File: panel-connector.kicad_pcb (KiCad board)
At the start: 2 copper layers, 95.9 x 90.2 mm, 72 parts, among them J1 PC104-8BIT, J10 MOLEX_FFC-14, J11 MOLEX_FFC-14, J12 CONN-TAB, J13 CONN-TAB, J14 CONN-TAB, J15 CONN-TAB, J16 MOLEX_FFC-14, J18 CONN-TAB, J19 CONN-TAB, J2 PC104PTH, J20 CONN-TAB, J21 CONN-TAB, J22 MOLEX_FFC-14, J24 CONN-TAB, J25 CONN-TAB, J26 CONN-TAB, J27 CONN-TAB, J28 MOLEX_FFC-14, J3 PC104PTH, J4 PC104PTH, J5 PC104PTH, J6 CONN-TAB, J7 CONN-TAB, J8 CONN-TAB, J9 CONN-TAB, U1 ADG728, U10 SPV1040, U11 SPV1040, U12 SPV1040, U2 ADG728, U3 ADG728, U4 ADG728, U5 SPV1040, U6 SPV1040, U7 SPV1040, U8 SPV1040, U9 SPV1040

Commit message: populated mppt schematic and layed out mppt circuit
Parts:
- removed J10, J11, J16, J22, J28: MOLEX_FFC-14, SFUSat:MOLEX_FFC-14
- removed U1, U2, U3, U4: ADG728, SFUSat:TSSOP-16
- added C10: 4u7F, SFUSat-cap:C_0805, F.Cu at (269.2, 97.7)
- added C11: 10uF, SFUSat-cap:C_0805, F.Cu at (255.7, 120.0)
- added C12: 100nF, SFUSat-cap:C_0805, F.Cu at (264.3, 119.6)
- added C13: 1n0F, SFUSat-cap:C_0805, F.Cu at (260.2, 119.8)
- added C14: 1u0F, SFUSat-cap:C_0805, F.Cu at (255.4, 123.7)
- added C15: 10uF, SFUSat-cap:C_0805, F.Cu at (259.5, 124.1)
- added C16: 4u7F, SFUSat-cap:C_0805, F.Cu at (263.5, 124.0)
- added C17: 10uF, SFUSat-cap:C_0805, F.Cu at (53.1, 93.7)
- added C18: 100nF, SFUSat-cap:C_0805, F.Cu at (53.0, 96.9)
- added C19: 1n0F, SFUSat-cap:C_0805, F.Cu at (52.7, 100.8)
- added C20: 1u0F, SFUSat-cap:C_0805, F.Cu at (58.4, 93.5)
- added C21: 10uF, SFUSat-cap:C_0805, F.Cu at (57.8, 97.1)
- added C22: 4u7F, SFUSat-cap:C_0805, F.Cu at (57.0, 100.8)
- added C23: 10uF, SFUSat-cap:C_0805, F.Cu at (50.2, 124.6)
- added C24: 100nF, SFUSat-cap:C_0805, F.Cu at (50.4, 128.2)
- added C25: 1n0F, SFUSat-cap:C_0805, F.Cu at (55.1, 124.6)
- added C26: 1u0F, SFUSat-cap:C_0805, F.Cu at (55.7, 128.4)
- added C27: 10uF, SFUSat-cap:C_0805, F.Cu at (59.7, 124.2)
- added C28: 4u7F, SFUSat-cap:C_0805, F.Cu at (60.5, 128.2)
- added C29: 10uF, SFUSat-cap:C_0805, F.Cu at (129.0, 170.3)
- added C30: 100nF, SFUSat-cap:C_0805, F.Cu at (128.6, 174.2)
- added C31: 1n0F, SFUSat-cap:C_0805, F.Cu at (123.3, 170.5)
- added C32: 1u0F, SFUSat-cap:C_0805, F.Cu at (123.3, 175.0)
- added C33: 10uF, SFUSat-cap:C_0805, F.Cu at (118.5, 170.3)
- added C34: 4u7F, SFUSat-cap:C_0805, F.Cu at (117.6, 174.8)
- added C35: 10uF, SFUSat-cap:C_0805, F.Cu at (130.0, 189.2)
- added C36: 100nF, SFUSat-cap:C_0805, F.Cu at (129.4, 193.3)
- added C37: 1n0F, SFUSat-cap:C_0805, F.Cu at (123.7, 189.0)
- added C38: 1u0F, SFUSat-cap:C_0805, F.Cu at (123.3, 193.1)
- added C39: 10uF, SFUSat-cap:C_0805, F.Cu at (117.4, 189.2)
- added C40: 4u7F, SFUSat-cap:C_0805, F.Cu at (118.7, 193.4)
- added C41: 10uF, SFUSat-cap:C_0805, F.Cu at (119.6, 19.6)
- added C42: 100nF, SFUSat-cap:C_0805, F.Cu at (119.7, 24.3)
- added C43: 1n0F, SFUSat-cap:C_0805, F.Cu at (124.1, 19.6)
- added C44: 1u0F, SFUSat-cap:C_0805, F.Cu at (124.4, 23.7)
- added C45: 10uF, SFUSat-cap:C_0805, F.Cu at (128.9, 18.2)
- added C46: 4u7F, SFUSat-cap:C_0805, F.Cu at (129.5, 23.2)
- added C47: 10uF, SFUSat-cap:C_0805, F.Cu at (135.5, 71.5)
- added C48: 100nF, SFUSat-cap:C_0805, F.Cu at (136.5, 74.2)
- added C49: 1n0F, SFUSat-cap:C_0805, F.Cu at (144.7, 81.2)
- added C5: 10uF, SFUSat-cap:C_0805, F.Cu at (265.7, 94.5)
- added C50: 1u0F, SFUSat-cap:C_0805, F.Cu at (142.9, 77.4)
- added C51: 10uF, SFUSat-cap:C_0805, F.Cu at (143.7, 84.0)
- added C52: 4u7F, SFUSat-cap:C_0805, F.Cu at (137.4, 81.4)
- added C6: 100nF, SFUSat-cap:C_0805, F.Cu at (261.9, 94.3)
- added C7: 1n0F, SFUSat-cap:C_0805, F.Cu at (261.3, 97.9)
- added C8: 1u0F, SFUSat-cap:C_0805, F.Cu at (269.8, 94.5)
- added C9: 10uF, SFUSat-cap:C_0805, F.Cu at (265.1, 97.8)
- added D1: SMM4F5.0A-TR, SFUSat:SMM4F, F.Cu at (277.0, 88.8)
- added D2: SMM4F5.0A-TR, SFUSat:SMM4F, F.Cu at (274.3, 112.8)
- added D3: SMM4F5.0A-TR, SFUSat:SMM4F, F.Cu at (36.7, 90.7)
- added D4: SMM4F5.0A-TR, SFUSat:SMM4F, F.Cu at (41.9, 132.1)
- added D5: SMM4F5.0A-TR, SFUSat:SMM4F, F.Cu at (135.5, 177.1)
- added D6: SMM4F5.0A-TR, SFUSat:SMM4F, F.Cu at (144.4, 186.3)
- added D7: SMM4F5.0A-TR, SFUSat:SMM4F, F.Cu at (112.6, 28.1)
- added D8: SMM4F5.0A-TR, SFUSat:SMM4F, F.Cu at (133.0, 82.4)
- added L1: L_10u0_10%_1.42A_2-SMD,, SFUSat-ind:L_2220, F.Cu at (260.3, 88.6)
- added L2: L_10u0_10%_1.42A_2-SMD,, SFUSat-ind:L_2220, F.Cu at (258.9, 113.3)
- added L3: L_10u0_10%_1.42A_2-SMD,, SFUSat-ind:L_2220, F.Cu at (35.2, 83.7)
- added L4: L_10u0_10%_1.42A_2-SMD,, SFUSat-ind:L_2220, F.Cu at (32.7, 126.2)
- added L5: L_10u0_10%_1.42A_2-SMD,, SFUSat-ind:L_2220, F.Cu at (146.9, 172.0)
- added L6: L_10u0_10%_1.42A_2-SMD,, SFUSat-ind:L_2220, F.Cu at (146.3, 192.7)
- added L7: L_10u0_10%_1.42A_2-SMD,, SFUSat-ind:L_2220, F.Cu at (101.6, 22.9)
- added L8: L_10u0_10%_1.42A_2-SMD,, SFUSat-ind:L_2220, F.Cu at (130.7, 76.7)
- added R27: 1K, SFUSat-res:R_0805, F.Cu at (274.1, 84.1)
- added R28: 0R, SFUSat-res:R_0402, F.Cu at (264.8, 79.6)
- added R29: 1k0, SFUSat-res:R_0805, F.Cu at (264.8, 82.0)
- added R30: 1k0, SFUSat-res:R_0805, F.Cu at (268.9, 79.3)
- added R31: 10m0, SFUSat-res:R_1206, F.Cu at (268.4, 81.4)
- added R32: 1M0, SFUSat-res:R_0805, F.Cu at (264.7, 83.8)
- added R33: 357k, SFUSat-res:R_0805, F.Cu at (268.6, 83.5)
- added R34: 1K, SFUSat-res:R_0805, F.Cu at (271.7, 117.9)
- added R35: 0R, SFUSat-res:R_0402, F.Cu at (274.6, 117.7)
- added R36: 1k0, SFUSat-res:R_0805, F.Cu at (277.5, 117.7)
- added R37: 1k0, SFUSat-res:R_0805, F.Cu at (271.9, 119.7)
- added R38: 10m0, SFUSat-res:R_1206, F.Cu at (276.1, 120.1)
- added R39: 1M0, SFUSat-res:R_0805, F.Cu at (271.5, 121.9)
- added R40: 357k, SFUSat-res:R_0805, F.Cu at (275.1, 122.2)
- added R41: 1K, SFUSat-res:R_0805, F.Cu at (35.4, 105.2)
- added R42: 0R, SFUSat-res:R_0402, F.Cu at (35.6, 103.7)
- added R43: 1k0, SFUSat-res:R_0805, F.Cu at (38.7, 103.4)
- added R44: 1k0, SFUSat-res:R_0805, F.Cu at (39.2, 105.1)
- added R45: 10m0, SFUSat-res:R_1206, F.Cu at (31.2, 104.7)
- added R46: 1M0, SFUSat-res:R_0805, F.Cu at (34.9, 102.4)
- added R47: 357k, SFUSat-res:R_0805, F.Cu at (31.5, 102.2)
- added R48: 1K, SFUSat-res:R_0805, F.Cu at (32.6, 134.1)
- added R49: 0R, SFUSat-res:R_0402, F.Cu at (29.8, 134.1)
- added R50: 1k0, SFUSat-res:R_0805, F.Cu at (36.0, 133.9)
- added R51: 1k0, SFUSat-res:R_0805, F.Cu at (35.9, 135.6)
- added R52: 10m0, SFUSat-res:R_1206, F.Cu at (32.4, 135.8)
- added R53: 1M0, SFUSat-res:R_0805, F.Cu at (28.7, 135.7)
- added R54: 357k, SFUSat-res:R_0805, F.Cu at (36.2, 137.2)
- added R55: 1K, SFUSat-res:R_0805, F.Cu at (129.5, 160.6)
- added R56: 0R, SFUSat-res:R_0402, F.Cu at (131.9, 160.4)
- added R57: 1k0, SFUSat-res:R_0805, F.Cu at (129.1, 162.3)
- added R58: 1k0, SFUSat-res:R_0805, F.Cu at (132.6, 162.2)
- added R59: 10m0, SFUSat-res:R_1206, F.Cu at (135.4, 160.4)
- added R60: 1M0, SFUSat-res:R_0805, F.Cu at (135.8, 162.3)
- added R61: 357k, SFUSat-res:R_0805, F.Cu at (126.0, 162.2)
- added R62: 1K, SFUSat-res:R_0805, F.Cu at (102.9, 190.7)
- added R63: 0R, SFUSat-res:R_0402, F.Cu at (109.0, 190.2)
- added R64: 1k0, SFUSat-res:R_0805, F.Cu at (106.5, 190.7)
- added R65: 1k0, SFUSat-res:R_0805, F.Cu at (111.7, 190.6)
- added R66: 10m0, SFUSat-res:R_1206, F.Cu at (102.3, 192.6)
- added R67: 1M0, SFUSat-res:R_0805, F.Cu at (105.9, 192.5)
- added R68: 357k, SFUSat-res:R_0805, F.Cu at (109.4, 192.6)
- added R69: 1K, SFUSat-res:R_0805, F.Cu at (102.0, 32.6)
- added R70: 0R, SFUSat-res:R_0402, F.Cu at (104.8, 32.0)
- added R71: 1k0, SFUSat-res:R_0805, F.Cu at (114.0, 31.9)
- added R72: 1k0, SFUSat-res:R_0805, F.Cu at (110.4, 33.1)
- added R73: 10m0, SFUSat-res:R_1206, F.Cu at (105.7, 34.7)
- added R74: 1M0, SFUSat-res:R_0805, F.Cu at (109.9, 35.2)
- added R75: 357k, SFUSat-res:R_0805, F.Cu at (113.8, 35.3)
- added R76: 1K, SFUSat-res:R_0805, F.Cu at (134.5, 74.2)
- added R77: 0R, SFUSat-res:R_0402, F.Cu at (139.6, 75.5)
- added R78: 1k0, SFUSat-res:R_0805, F.Cu at (145.8, 76.5)
- added R79: 1k0, SFUSat-res:R_0805, F.Cu at (145.8, 78.4)
- added R80: 10m0, SFUSat-res:R_1206, F.Cu at (137.9, 83.6)
- added R81: 1M0, SFUSat-res:R_0805, F.Cu at (142.7, 81.2)
- added R82: 357k, SFUSat-res:R_0805, F.Cu at (146.6, 81.2)
- moved U12 54.9 mm to (137.5, 78.1)
- moved U8 23.0 mm to (42.8, 126.0)
- moved U10 13.6 mm to (137.4, 192.3)
- moved U6 12.8 mm to (268.0, 112.7)
- moved U7 8.33 mm to (44.6, 86.7)
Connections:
- net /3V3 renamed /Port_X+/3V3
- net /SCL renamed /Port_X+/SCL
- net /SDA renamed /Port_X+/SDA
- net /SENSOR_X+ renamed /Port_X+/SUN_SENSOR
- net /SENSOR_X- renamed /Port_X-/SUN_SENSOR
- net /SENSOR_Y+ renamed /Port_Y+/SUN_SENSOR
- net /SENSOR_Y- renamed /Port_Y-/SUN_SENSOR
- U11 pad 2: GND -> /MPPT_Y-_1/PV-
- U5 pad 2: GND -> /MPPT_X+_1/PV-
- U7 pad 2: GND -> /MPPT_X-_1/PV-
- U9 pad 2: GND -> /MPPT_Y+_1/PV-
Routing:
- net Net-(C52-Pad1): track 0.00 -> 17.4 mm, vias 0 -> 2
- net /MPPT_Y-_1/PV-: track 0.00 -> 10.7 mm, vias 0 -> 2
- net GND: track 0.00 -> 9.21 mm, vias 0 -> 8
- net Net-(C49-Pad1): track 0.00 -> 6.69 mm
- net Net-(C48-Pad1): track 0.00 -> 6.64 mm
- net Net-(C50-Pad1): track 0.00 -> 4.89 mm
- net Net-(C50-Pad2): track 0.00 -> 4.32 mm
- net Net-(R77-Pad1): track 0.00 -> 1.78 mm
- added copper zone on F.Cu, net /MPPT_Y-_1/PV-
- added copper zone on F.Cu, net /MPPT_Y-_2/PV+
- added copper zone on B.Cu, net GND
- added copper zone on F.Cu, net Net-(C52-Pad1)
- added copper zone on F.Cu, net Net-(L8-Pad2)
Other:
- net class PV_PWR added: clearance 0.2, trace_width 0.4, via_dia 0.6, via_drill 0.4
- rule trace_min: 0.2 -> 0.1524

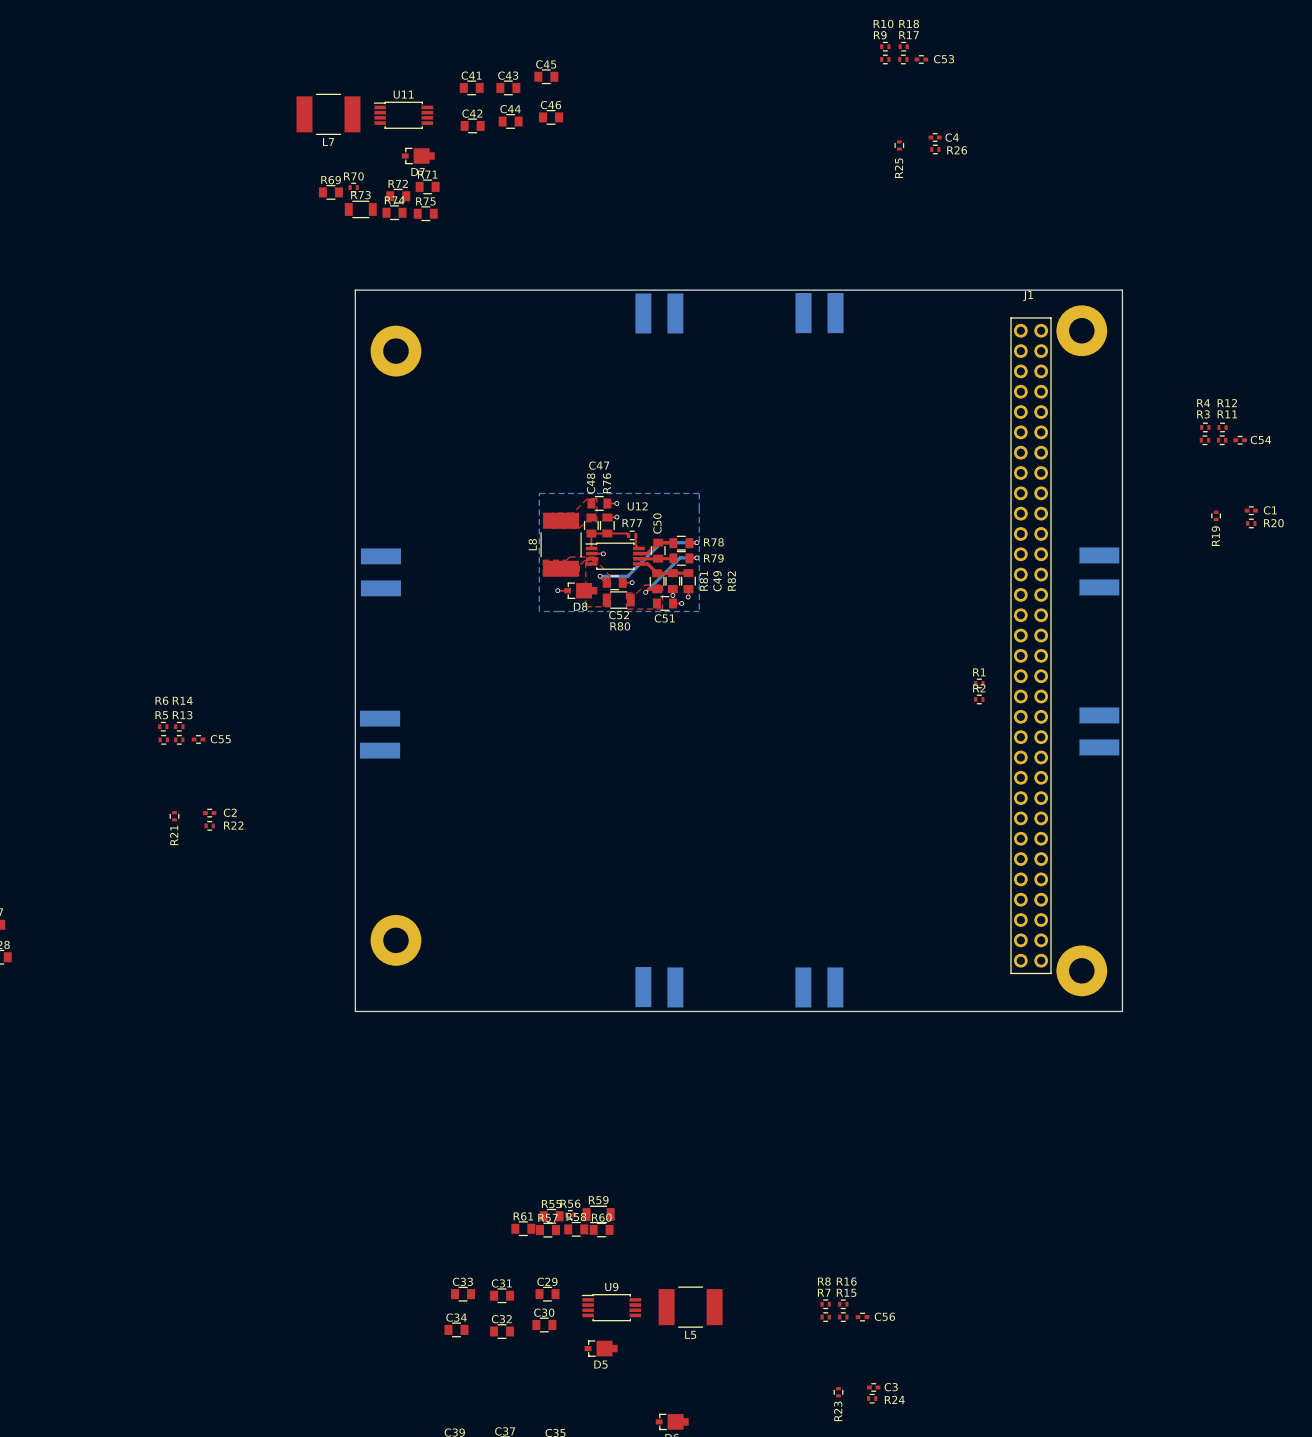
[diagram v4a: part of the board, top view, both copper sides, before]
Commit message: Added decoupling to connector
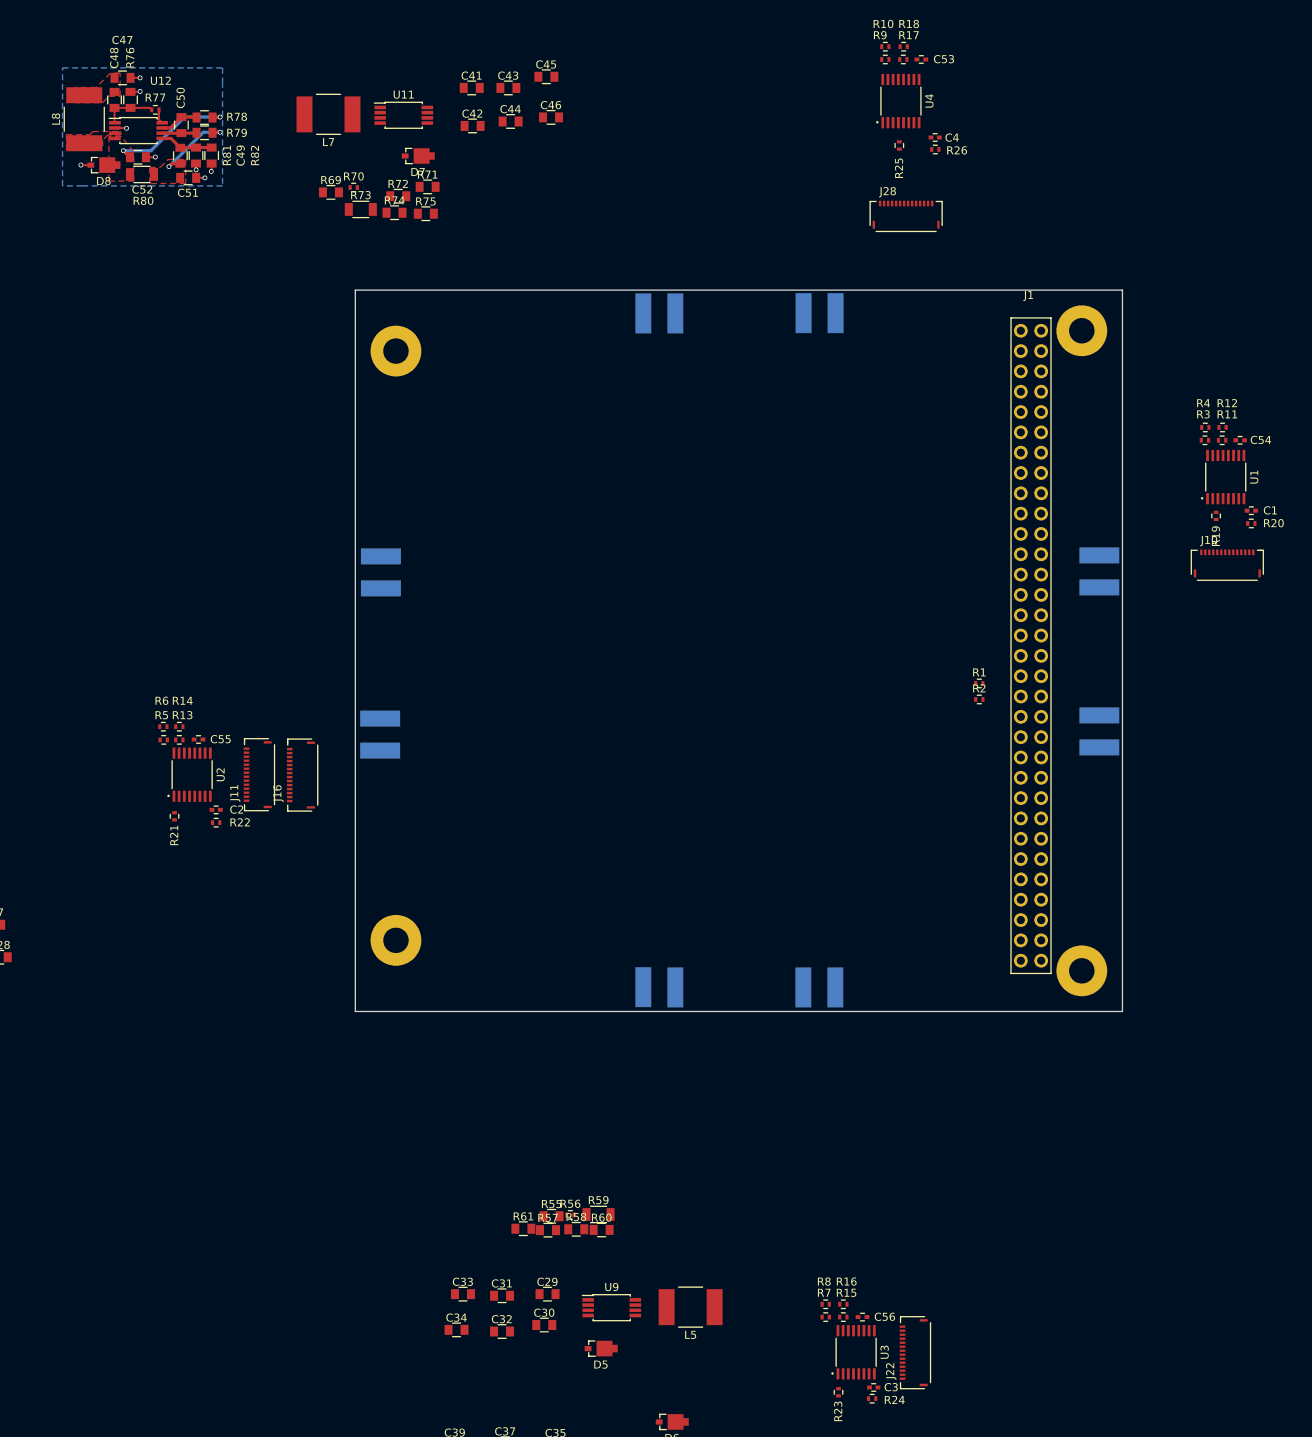
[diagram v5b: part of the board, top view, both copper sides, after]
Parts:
- added J10: MOLEX_FFC-14, SFUSat:MOLEX_FFC-14, F.Cu at (214.0, 77.6)
- added J11: MOLEX_FFC-14, SFUSat:MOLEX_FFC-14, F.Cu at (91.4, 105.4)
- added J16: MOLEX_FFC-14, SFUSat:MOLEX_FFC-14, F.Cu at (96.8, 105.5)
- added J22: MOLEX_FFC-14, SFUSat:MOLEX_FFC-14, F.Cu at (173.4, 177.7)
- added J28: MOLEX_FFC-14, SFUSat:MOLEX_FFC-14, F.Cu at (173.8, 34.0)
- added U1: ADG728, SFUSat:TSSOP-16, F.Cu at (213.8, 68.2)
- added U2: ADG728, SFUSat:TSSOP-16, F.Cu at (84.6, 105.4)
- added U3: ADG728, SFUSat:TSSOP-16, F.Cu at (167.6, 177.6)
- added U4: ADG728, SFUSat:TSSOP-16, F.Cu at (173.2, 21.2)
- moved C49 79.9 mm to (85.1, 28.0)
- moved C50 79.9 mm to (83.3, 24.2)
- moved C52 79.9 mm to (77.8, 28.2)
- moved L8 79.9 mm to (71.1, 23.5)
- moved R79 79.9 mm to (86.2, 25.2)
- moved R78 79.9 mm to (86.2, 23.3)
- moved U12 79.9 mm to (77.9, 24.9)
- moved C47 79.9 mm to (75.9, 18.3)
- moved C48 79.9 mm to (76.9, 21.1)
- moved C51 79.9 mm to (84.1, 30.8)
- moved D8 79.9 mm to (73.4, 29.2)
- moved R76 79.9 mm to (74.9, 21.1)
- moved R77 79.9 mm to (80.0, 22.3)
- moved R80 79.9 mm to (78.3, 30.4)
- moved R81 79.9 mm to (83.1, 28.0)
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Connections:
- net /Port_X+/3V3 renamed /3V3
- net /Port_X+/SCL renamed /SCL
- net /Port_X+/SDA renamed /SDA
- net /Port_X+/SUN_SENSOR renamed /SENSOR_X+
- net /Port_X-/SUN_SENSOR renamed /SENSOR_X-
- net /Port_Y+/SUN_SENSOR renamed /SENSOR_Y+
- net /Port_Y-/SUN_SENSOR renamed /SENSOR_Y-

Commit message: layed out MPPT
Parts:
- removed C10: 4u7F, SFUSat-cap:C_0805
- removed C5, C9: 10uF, SFUSat-cap:C_0805
- removed C6: 100nF, SFUSat-cap:C_0805
- removed C7: 1n0F, SFUSat-cap:C_0805
- removed C8: 1u0F, SFUSat-cap:C_0805
- added C100: 10uF, SFUSat-cap:C_0805, F.Cu at (249.9, -19.7)
- added C101: 100nF, SFUSat-cap:C_0805, F.Cu at (250.9, -16.9)
- added C102: 1n0F, SFUSat-cap:C_0805, F.Cu at (259.1, -9.95)
- added C103: 1u0F, SFUSat-cap:C_0805, F.Cu at (257.3, -13.8)
- added C104: 10uF, SFUSat-cap:C_0805, F.Cu at (258.1, -7.16)
- added C105: 4u7F, SFUSat-cap:C_0805, F.Cu at (251.8, -9.74)
- added C200: DNP, Capacitors_SMD:C_0402, F.Cu at (261.5, 68.0)
- added C203: DNP, Capacitors_SMD:C_0402, F.Cu at (254.5, 68.0)
- added C210: DNP, Capacitors_SMD:C_0402, F.Cu at (261.3, 97.9)
- added C213: DNP, Capacitors_SMD:C_0402, F.Cu at (269.8, 94.5)
- added C220: DNP, Capacitors_SMD:C_0402, F.Cu at (265.1, 97.8)
- added C223: DNP, Capacitors_SMD:C_0402, F.Cu at (269.2, 97.7)
- added C230, C233: DNP, Capacitors_SMD:C_0402, F.Cu at (152.9, 145.1)
- moved L150 232.5 mm to (85.1, -31.5), turned to 270 degrees
- moved C151 230.5 mm to (90.9, -34.0), turned to 90 degrees
- moved C150 229.5 mm to (89.9, -36.7)
- moved U150 227.0 mm to (91.9, -30.1)
- moved C153 225.4 mm to (97.3, -30.8), turned to 270 degrees
- moved R150 225.1 mm to (88.9, -34.0), turned to 270 degrees
- moved R151 223.4 mm to (94.0, -32.7), turned to 180 degrees
- moved R152 222.5 mm to (100.2, -31.7), turned to 180 degrees
- moved C155 221.9 mm to (91.8, -26.8)
- moved R153 220.7 mm to (100.2, -29.8), turned to 180 degrees
- moved R131 220.5 mm to (174.0, -32.7), turned to 180 degrees
- moved R135 220.2 mm to (177.1, -27.0), turned to 90 degrees
- moved R156 219.8 mm to (101.0, -27.0), turned to 270 degrees
- moved D150 219.6 mm to (87.4, -25.8)
- moved R132 219.6 mm to (180.2, -31.7), turned to 180 degrees
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- renumbered C11 to C110, C12 to C111, C13 to C112, C14 to C113, C15 to C114, C16 to C115, C17 to C120, C18 to C121, C19 to C122, C20 to C123, C21 to C124, C22 to C125, C23 to C130, C24 to C131, C25 to C132, C26 to C133, C27 to C134, C28 to C135, C29 to C140, C30 to C141, C31 to C142, C32 to C143, C33 to C144, C34 to C145, C35 to C150, C36 to C151, C37 to C152, C38 to C153, C39 to C154, C40 to C155, C41 to C160, C42 to C161, C43 to C162, C44 to C163, C45 to C164, C46 to C165, C47 to C170, C48 to C171, C49 to C172, C50 to C173, C51 to C174, C52 to C175, C54 to C201, C1 to C202, C55 to C211, C2 to C212, C56 to C221, C3 to C222, C53 to C231, C4 to C232, D1 to D100, D2 to D110, D3 to D120, D4 to D130, D5 to D140, D6 to D150, D7 to D160, D8 to D170, J11 to J105, J10 to J200, J6 to J201, J7 to J202, J8 to J203, J9 to J204, J16 to J210, J12 to J211, J13 to J212, J14 to J213, J15 to J214, J22 to J220, J18 to J221, J19 to J222, J20 to J223, J21 to J224, J28 to J230, J24 to J231, J25 to J232, J26 to J233, J27 to J234, L1 to L100, L2 to L110, L3 to L120, L4 to L130, L5 to L140, L6 to L150, L7 to L160, L8 to L170, R27 to R100, R28 to R101, R29 to R102, R30 to R103, R31 to R104, R32 to R105, R33 to R106, R34 to R110, R35 to R111, R36 to R112, R37 to R113, R38 to R114, R39 to R115, R40 to R116, R41 to R120, R42 to R121, R43 to R122, R44 to R123, R45 to R124, R46 to R125, R47 to R126, R48 to R130, R49 to R131, R50 to R132, R51 to R133, R52 to R134, R53 to R135, R54 to R136, R55 to R140, R56 to R141, R57 to R142, R58 to R143, R59 to R144, R60 to R145, R61 to R146, R62 to R150, R63 to R151, R64 to R152, R65 to R153, R66 to R154, R67 to R155, R68 to R156, R69 to R160, R70 to R161, R71 to R162, R72 to R163, R73 to R164, R74 to R165, R75 to R166, R76 to R170, R77 to R171, R78 to R172, R79 to R173, R80 to R174, R81 to R175, R82 to R176, R20 to R200, R19 to R201'1, R3 to R202, R11 to R203, R4 to R204, R12 to R205, R22 to R210, R21 to R211, R5 to R212, R13 to R213, R6 to R214, R14 to R215, R24 to R220, R23 to R221, R7 to R222, R15 to R223, R8 to R224, R16 to R225, R26 to R230, R25 to R231, R9 to R232, R17 to R233, R10 to R234, R18 to R235, U5 to U100, U6 to U110, U7 to U120, U8 to U130, U9 to U140, U10 to U150, U11 to U160, U12 to U170, U1 to U200, U2 to U210, U3 to U220, U4 to U230
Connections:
- net Net-(L1-Pad2) renamed /MPPT_X+_1/LX
- net Net-(L2-Pad2) renamed /MPPT_X+_2/LX
- net Net-(L3-Pad2) renamed /MPPT_X-_1/LX
- net Net-(L4-Pad2) renamed /MPPT_X-_2/LX
- net Net-(L5-Pad2) renamed /MPPT_Y+_1/LX
- net Net-(L6-Pad2) renamed /MPPT_Y+_2/LX
- net Net-(L7-Pad2) renamed /MPPT_Y-_1/LX
- net Net-(L8-Pad2) renamed /MPPT_Y-_2/LX
- C113 pad 1: Net-(C14-Pad1) -> Net-(C113-Pad1)
- C113 pad 2: Net-(C14-Pad2) -> Net-(C113-Pad2)
- C115 pad 1: Net-(C16-Pad1) -> /MPPT_X+_2/MPPT_OUT
- C123 pad 1: Net-(C20-Pad1) -> Net-(C123-Pad1)
- C123 pad 2: Net-(C20-Pad2) -> Net-(C123-Pad2)
- C125 pad 1: Net-(C22-Pad1) -> /MPPT_X-_1/MPPT_OUT
- C133 pad 1: Net-(C26-Pad1) -> Net-(C133-Pad1)
- C133 pad 2: Net-(C26-Pad2) -> Net-(C133-Pad2)
- C135 pad 1: Net-(C28-Pad1) -> /MPPT_X-_2/MPPT_OUT
- C143 pad 1: Net-(C32-Pad1) -> Net-(C143-Pad1)
- C143 pad 2: Net-(C32-Pad2) -> Net-(C143-Pad2)
- C145 pad 1: Net-(C34-Pad1) -> /MPPT_Y+_1/MPPT_OUT
- C153 pad 1: Net-(C38-Pad1) -> Net-(C153-Pad1)
- C153 pad 2: Net-(C38-Pad2) -> Net-(C153-Pad2)
- C155 pad 1: Net-(C40-Pad1) -> /MPPT_Y+_2/MPPT_OUT
- C163 pad 1: Net-(C44-Pad1) -> Net-(C163-Pad1)
- C163 pad 2: Net-(C44-Pad2) -> Net-(C163-Pad2)
- C165 pad 1: Net-(C46-Pad1) -> /MPPT_Y-_1/MPPT_OUT
- C173 pad 1: Net-(C50-Pad1) -> Net-(C173-Pad1)
- C173 pad 2: Net-(C50-Pad2) -> Net-(C173-Pad2)
- C175 pad 1: Net-(C52-Pad1) -> /MPPT_Y-_2/MPPT_OUT
- D100 pad C: Net-(C10-Pad1) -> /MPPT_X+_1/MPPT_OUT
- D110 pad C: Net-(C16-Pad1) -> /MPPT_X+_2/MPPT_OUT
- D120 pad C: Net-(C22-Pad1) -> /MPPT_X-_1/MPPT_OUT
- D130 pad C: Net-(C28-Pad1) -> /MPPT_X-_2/MPPT_OUT
- D140 pad C: Net-(C34-Pad1) -> /MPPT_Y+_1/MPPT_OUT
- D150 pad C: Net-(C40-Pad1) -> /MPPT_Y+_2/MPPT_OUT
- D160 pad C: Net-(C46-Pad1) -> /MPPT_Y-_1/MPPT_OUT
- D170 pad C: Net-(C52-Pad1) -> /MPPT_Y-_2/MPPT_OUT
- J201 pad 1: Net-(J6-Pad1) -> /MPPT_X+_1/PV+
- J202 pad 1: Net-(J7-Pad1) -> /MPPT_X+_1/PV-
- J203 pad 1: Net-(J8-Pad1) -> /MPPT_X+_2/PV+
- J204 pad 1: Net-(J9-Pad1) -> GND
- J211 pad 1: Net-(J12-Pad1) -> /MPPT_X-_1/PV+
- J212 pad 1: Net-(J13-Pad1) -> /MPPT_X-_1/PV-
- J213 pad 1: Net-(J14-Pad1) -> /MPPT_X-_2/PV+
- J214 pad 1: Net-(J15-Pad1) -> GND
- J221 pad 1: Net-(J18-Pad1) -> /MPPT_Y+_1/PV+
- J222 pad 1: Net-(J19-Pad1) -> /MPPT_Y+_1/PV-
- J223 pad 1: Net-(J20-Pad1) -> /MPPT_Y+_2/PV+
- J224 pad 1: Net-(J21-Pad1) -> GND
- J231 pad 1: Net-(J24-Pad1) -> /MPPT_Y-_2/PV+
- J232 pad 1: Net-(J25-Pad1) -> GND
- J233 pad 1: Net-(J26-Pad1) -> /MPPT_Y-_1/PV+
- J234 pad 1: Net-(J27-Pad1) -> /MPPT_Y-_1/PV-
- R102 pad 1: Net-(C8-Pad1) -> /MPPT_X+_1/MPPT_OUT
- R102 pad 2: Net-(C10-Pad1) -> Net-(C103-Pad1)
- R103 pad 1: Net-(C8-Pad2) -> /MPPT_X+_1/VOUT+
- R103 pad 2: /MPPT_X+_1/VOUT+ -> Net-(C103-Pad2)
- R104 pad 1: Net-(C10-Pad1) -> /MPPT_X+_1/MPPT_OUT
- R112 pad 1: Net-(C14-Pad1) -> /MPPT_X+_2/MPPT_OUT
- R112 pad 2: Net-(C16-Pad1) -> Net-(C113-Pad1)
- R113 pad 1: Net-(C14-Pad2) -> /MPPT_X+_1/PV-
- R113 pad 2: /MPPT_X+_1/PV- -> Net-(C113-Pad2)
- R114 pad 1: Net-(C16-Pad1) -> /MPPT_X+_2/MPPT_OUT
- R122 pad 1: Net-(C20-Pad1) -> /MPPT_X-_1/MPPT_OUT
- R122 pad 2: Net-(C22-Pad1) -> Net-(C123-Pad1)
- R123 pad 1: Net-(C20-Pad2) -> /MPPT_X+_1/VOUT+
- R123 pad 2: /MPPT_X+_1/VOUT+ -> Net-(C123-Pad2)
- R124 pad 1: Net-(C22-Pad1) -> /MPPT_X-_1/MPPT_OUT
- R132 pad 1: Net-(C26-Pad1) -> /MPPT_X-_2/MPPT_OUT
- R132 pad 2: Net-(C28-Pad1) -> Net-(C133-Pad1)
- R133 pad 1: Net-(C26-Pad2) -> /MPPT_X-_1/PV-
- R133 pad 2: /MPPT_X-_1/PV- -> Net-(C133-Pad2)
- R134 pad 1: Net-(C28-Pad1) -> /MPPT_X-_2/MPPT_OUT
- R142 pad 1: Net-(C32-Pad1) -> /MPPT_Y+_1/MPPT_OUT
- R142 pad 2: Net-(C34-Pad1) -> Net-(C143-Pad1)
- R143 pad 1: Net-(C32-Pad2) -> /MPPT_X+_1/VOUT+
- R143 pad 2: /MPPT_X+_1/VOUT+ -> Net-(C143-Pad2)
- R144 pad 1: Net-(C34-Pad1) -> /MPPT_Y+_1/MPPT_OUT
- R152 pad 1: Net-(C38-Pad1) -> /MPPT_Y+_2/MPPT_OUT
- R152 pad 2: Net-(C40-Pad1) -> Net-(C153-Pad1)
- R153 pad 1: Net-(C38-Pad2) -> /MPPT_Y+_1/PV-
- R153 pad 2: /MPPT_Y+_1/PV- -> Net-(C153-Pad2)
- R154 pad 1: Net-(C40-Pad1) -> /MPPT_Y+_2/MPPT_OUT
- R162 pad 1: Net-(C44-Pad1) -> /MPPT_Y-_1/MPPT_OUT
- R162 pad 2: Net-(C46-Pad1) -> Net-(C163-Pad1)
- R163 pad 1: Net-(C44-Pad2) -> /MPPT_X+_1/VOUT+
- R163 pad 2: /MPPT_X+_1/VOUT+ -> Net-(C163-Pad2)
- R164 pad 1: Net-(C46-Pad1) -> /MPPT_Y-_1/MPPT_OUT
- R172 pad 1: Net-(C50-Pad1) -> /MPPT_Y-_2/MPPT_OUT
- R172 pad 2: Net-(C52-Pad1) -> Net-(C173-Pad1)
- R173 pad 1: Net-(C50-Pad2) -> /MPPT_Y-_1/PV-
- R173 pad 2: /MPPT_Y-_1/PV- -> Net-(C173-Pad2)
- R174 pad 1: Net-(C52-Pad1) -> /MPPT_Y-_2/MPPT_OUT
- U100 pad 4: Net-(C10-Pad1) -> /MPPT_X+_1/MPPT_OUT
- U100 pad 6: Net-(C8-Pad2) -> Net-(C103-Pad2)
- U100 pad 7: Net-(C8-Pad1) -> Net-(C103-Pad1)
- U110 pad 4: Net-(C16-Pad1) -> /MPPT_X+_2/MPPT_OUT
- U110 pad 6: Net-(C14-Pad2) -> Net-(C113-Pad2)
- U110 pad 7: Net-(C14-Pad1) -> Net-(C113-Pad1)
- U120 pad 4: Net-(C22-Pad1) -> /MPPT_X-_1/MPPT_OUT
- U120 pad 6: Net-(C20-Pad2) -> Net-(C123-Pad2)
- U120 pad 7: Net-(C20-Pad1) -> Net-(C123-Pad1)
- U130 pad 4: Net-(C28-Pad1) -> /MPPT_X-_2/MPPT_OUT
- U130 pad 6: Net-(C26-Pad2) -> Net-(C133-Pad2)
- U130 pad 7: Net-(C26-Pad1) -> Net-(C133-Pad1)
- U140 pad 4: Net-(C34-Pad1) -> /MPPT_Y+_1/MPPT_OUT
- U140 pad 6: Net-(C32-Pad2) -> Net-(C143-Pad2)
- U140 pad 7: Net-(C32-Pad1) -> Net-(C143-Pad1)
- U150 pad 4: Net-(C40-Pad1) -> /MPPT_Y+_2/MPPT_OUT
- U150 pad 6: Net-(C38-Pad2) -> Net-(C153-Pad2)
- U150 pad 7: Net-(C38-Pad1) -> Net-(C153-Pad1)
- U160 pad 4: Net-(C46-Pad1) -> /MPPT_Y-_1/MPPT_OUT
- U160 pad 6: Net-(C44-Pad2) -> Net-(C163-Pad2)
- U160 pad 7: Net-(C44-Pad1) -> Net-(C163-Pad1)
- U170 pad 4: Net-(C52-Pad1) -> /MPPT_Y-_2/MPPT_OUT
- U170 pad 6: Net-(C50-Pad2) -> Net-(C173-Pad2)
- U170 pad 7: Net-(C50-Pad1) -> Net-(C173-Pad1)
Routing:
- net /MPPT_X+_1/VOUT+: track 0.00 -> 43.4 mm, vias 0 -> 8
- net GND: track 9.21 -> 36.9 mm, vias 8 -> 32
- net (no net): track 0.00 -> 26.0 mm
- net /MPPT_X+_1/PV-: track 0.00 -> 20.1 mm, vias 0 -> 10
- net /MPPT_X-_1/PV-: track 0.00 -> 20.1 mm, vias 0 -> 10
- net /MPPT_Y+_1/PV-: track 0.00 -> 20.1 mm, vias 0 -> 10
- net Net-(C52-Pad1): track 17.4 -> 0.00 mm, vias 2 -> 0
- net /MPPT_X-_2/MPPT_OUT: track 0.00 -> 15.5 mm, vias 0 -> 2
- net /MPPT_X-_1/MPPT_OUT: track 0.00 -> 15.5 mm, vias 0 -> 2
- net /MPPT_X+_2/MPPT_OUT: track 0.00 -> 15.5 mm, vias 0 -> 2
- net /MPPT_X+_1/MPPT_OUT: track 0.00 -> 15.5 mm, vias 0 -> 2
- net /MPPT_Y+_2/MPPT_OUT: track 0.00 -> 15.5 mm, vias 0 -> 2
- net /MPPT_Y+_1/MPPT_OUT: track 0.00 -> 15.5 mm, vias 0 -> 2
- net /MPPT_Y-_2/MPPT_OUT: track 0.00 -> 15.5 mm, vias 0 -> 2
- net /MPPT_Y-_1/MPPT_OUT: track 0.00 -> 15.5 mm, vias 0 -> 2
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- added copper zone on F.Cu, net /MPPT_X+_1/LX
- added copper zone on F.Cu, net /MPPT_X+_1/MPPT_OUT
- added copper zone on F.Cu, net /MPPT_X+_1/PV+
- added copper zone on B.Cu, net /MPPT_X+_1/PV-
- added copper zone on F.Cu, net /MPPT_X+_1/PV-
- added copper zone on F.Cu, net /MPPT_X+_1/VOUT+
- added copper zone on F.Cu, net /MPPT_X+_2/LX
- added copper zone on F.Cu, net /MPPT_X+_2/MPPT_OUT
- added copper zone on F.Cu, net /MPPT_X+_2/PV+
- added copper zone on F.Cu, net /MPPT_X-_1/LX
- added copper zone on F.Cu, net /MPPT_X-_1/MPPT_OUT
- added copper zone on F.Cu, net /MPPT_X-_1/PV+
- added copper zone on B.Cu, net /MPPT_X-_1/PV-
- added copper zone on F.Cu, net /MPPT_X-_1/PV-
- added copper zone on F.Cu, net /MPPT_X-_2/LX
- added copper zone on F.Cu, net /MPPT_X-_2/MPPT_OUT
- added copper zone on F.Cu, net /MPPT_X-_2/PV+
- added copper zone on F.Cu, net /MPPT_Y+_1/LX
- added copper zone on F.Cu, net /MPPT_Y+_1/MPPT_OUT
- added copper zone on F.Cu, net /MPPT_Y+_1/PV+
- added copper zone on B.Cu, net /MPPT_Y+_1/PV-
- added copper zone on F.Cu, net /MPPT_Y+_1/PV-
- added copper zone on F.Cu, net /MPPT_Y+_2/LX
- added copper zone on F.Cu, net /MPPT_Y+_2/MPPT_OUT
- added copper zone on F.Cu, net /MPPT_Y+_2/PV+
- added copper zone on F.Cu, net /MPPT_Y-_1/LX
- added copper zone on F.Cu, net /MPPT_Y-_1/MPPT_OUT
- added copper zone on F.Cu, net /MPPT_Y-_1/PV+
- added copper zone on B.Cu, net /MPPT_Y-_1/PV-
- added copper zone on F.Cu, net /MPPT_Y-_2/MPPT_OUT
- removed copper zone on F.Cu, net Net-(C52-Pad1)
